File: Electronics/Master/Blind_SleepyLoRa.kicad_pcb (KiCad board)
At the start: 2 copper layers, 130.5 x 39.5 mm, 12 parts, among them J1 Conn_01x04_Socket, J2 Conn_01x04_Socket, J3 Conn_01x04_Socket, SW1 SW_Omron_B3FS

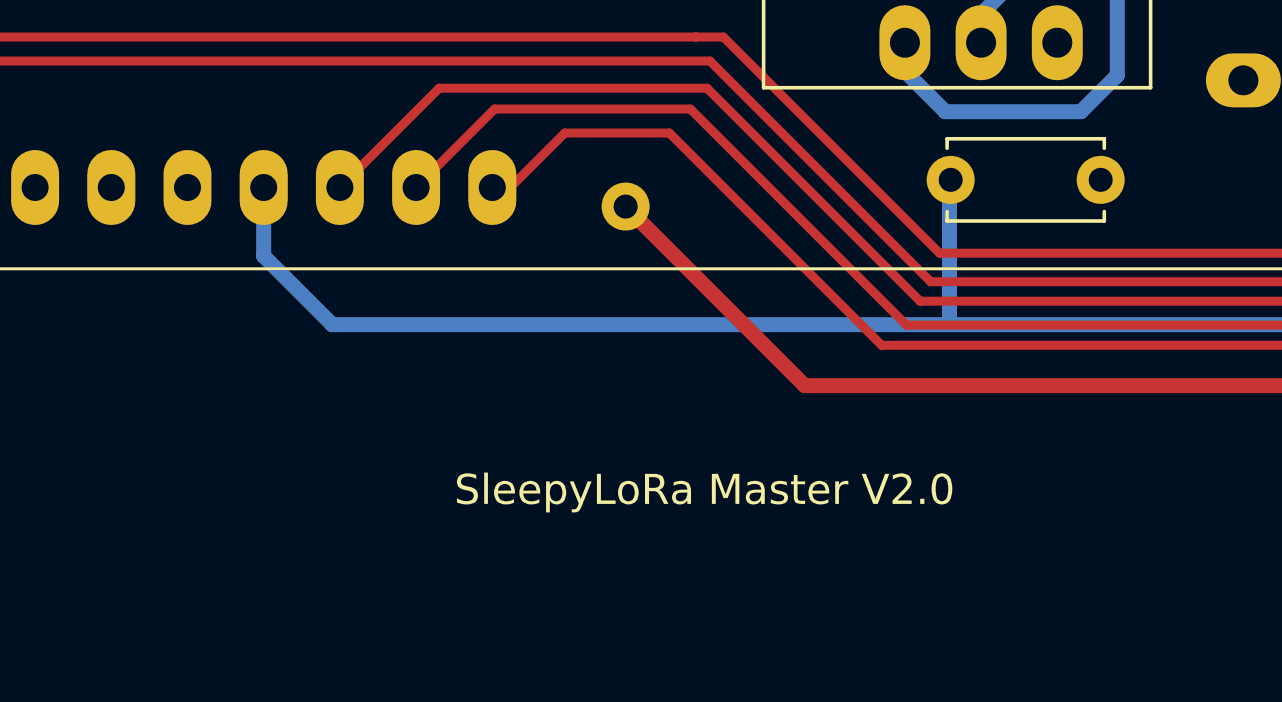
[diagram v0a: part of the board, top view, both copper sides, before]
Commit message: Update master PCB to include ref voltage
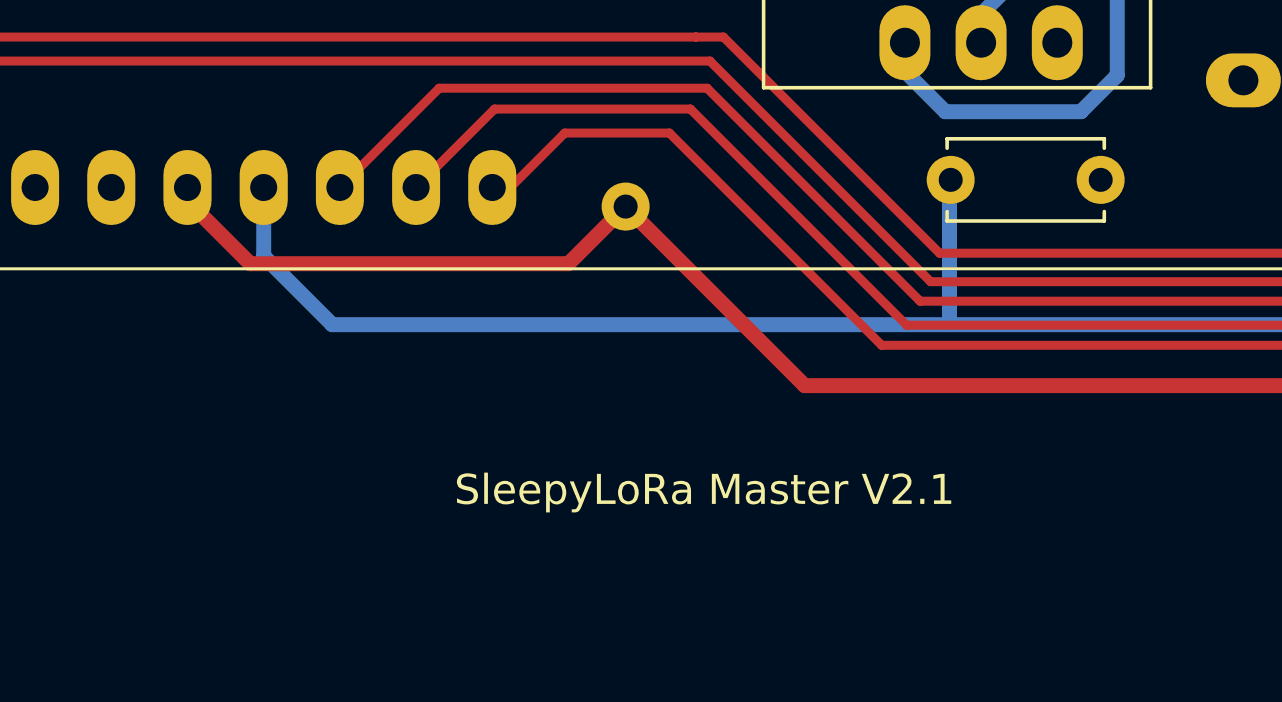
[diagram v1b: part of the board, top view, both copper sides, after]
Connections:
- U2 pad 25: unconnected-(U2-GPIO15-Pad25) -> /p1
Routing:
- net /p1: track 70.1 -> 86.9 mm
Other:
- board text added: "SleepyLoRa Master V2.1"
- board text removed: "SleepyLoRa Master V2.0"
